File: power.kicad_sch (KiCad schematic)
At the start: 0 parts

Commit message: add comments/todos for each schematics page
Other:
- note added: "Power - PSU-DC/DC Converter - 8-12V->5V: XL1509-5.0E1 - 5->3.3V: SY8113BADCCopy - Automatic Switch between 5V-Extern and 5V-USB"
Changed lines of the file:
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@@
     (company "Juventus Technikerschule")
   )
+  (text "Power\n- PSU-DC/DC Converter\n- 8-12V->5V: XL1509-5.0E1\n- 5->3.3V: SY8113BADCCopy\n- Automatic Switch between 5V-Extern and 5V-USB"
+    (at 13.97 24.13 0)
+    (effects (font (size 1.27 1.27)) (justify left bottom))
+  )
 )

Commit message: updated library, partly created power.kicad_sch
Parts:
- added C? (x3): 10uF, X5R, 25V, C0603, symbol eduboardv2:CL10A106MA8NRNC
- added C? (x3): 220uF, 35V, CAP-SMD_BD8.0-L8.3-W8.3-RD, symbol eduboardv2:VEJ221M1VTR-0810
- added C? (x3): 100nF, 50V, C0402, symbol eduboardv2:CL05B104KB54PNC
- added C? (x2): 1uF, 25V, C0402, symbol eduboardv2:CL05A105KA5NQNC
- added C?: 22pF, C0402, symbol eduboardv2:0402CG220J500NT
- added D?: SS210, SMA_L4.3-W2.6-LS5.2-RD, symbol eduboardv2:SS210
- added IC301: XL1509-5.0E1, SOIC-8_L5.0-W4.0-P1.27-LS6.0-BL, symbol eduboardv2:XL1509-5.0E1
- added L?: 6.8uH, 1A, IND-SMD_L4.0-W4.0, symbol eduboardv2:SWPA4020S6R8MT
- added L?: 68uH, 1A, IND-SMD_L6.0-W6.0_FNR60XXS, symbol eduboardv2:SWPA6045S680MT
- added R? (x2): 5.1k, R0402, symbol eduboardv2:0402WGF5101TCE
- added R? (x2): 100k, R0402, symbol eduboardv2:0402WGF1003TCE
- added R?: 22k, R0402, symbol eduboardv2:0402WGF2202TCE
- added U?: SY8113BADC, TSOT-23-6_L2.9-W1.6-P0.95-LS2.8-BR, symbol eduboardv2:SY8113BADC
- added USBC?: USB3.1C16PFSMT, USB-C-SMD_TYPE-C-USB-17, symbol eduboardv2:USB3.1C16PFSMT
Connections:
- new net: C?.2, L?.1, U?.6 (LX)
- new net: D?.1 (K), IC301.2 (OUTPUT), L?.1
- new net: R?.2, USBC?.A5 (CC1)
- new net: R?.1, USBC?.B5 (CC2)
- new net: C?.1, R?.1, R?.2, U?.3 (FB)
- new net: C?.1, U?.1 (BS)
- new net +3.3V: C?.1, C?.1, C?.1, C?.2, C?.2, L?.2, R?.2
- new net +5V: C?.1, C?.1, C?.1, C?.2, C?.2, IC301.3 (FB), L?.2, R?.2, U?.5 (IN)
- new net 3.3V_EN: R?.1, U?.4 (EN)
- new net GND: C?.1, C?.1, C?.1, C?.2, C?.2, C?.2, C?.2, C?.2, C?.2, C?.2, D?.2 (A), IC301.5 (GND), IC301.6 (GND), IC301.7 (GND), IC301.8 (GND), R?.1, R?.1, R?.2, U?.2 (GND), USBC?.A1 (GND), USBC?.A12 (GND)
- new net V_EXT: C?.1, IC301.1 (VIN)
- new net V_USB: USBC?.A4 (VBUS), USBC?.A9 (VBUS)

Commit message: nearly finished display_ui.kicad_sch and power.kicad_sch
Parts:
- added D? (x2): SS210, SMA_L4.3-W2.6-LS5.2-RD, symbol eduboardv2:SS210
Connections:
- net +5V: now also D?.1 (K), D?.1 (K); no longer C?.1, C?.1, C?.1, C?.2, IC301.3 (FB), L?.2
- net V_USB: now also D?.2 (A)
- new net +5V_EXT: C?.1, C?.1, C?.1, C?.2, D?.2 (A), IC301.3 (FB), L?.2

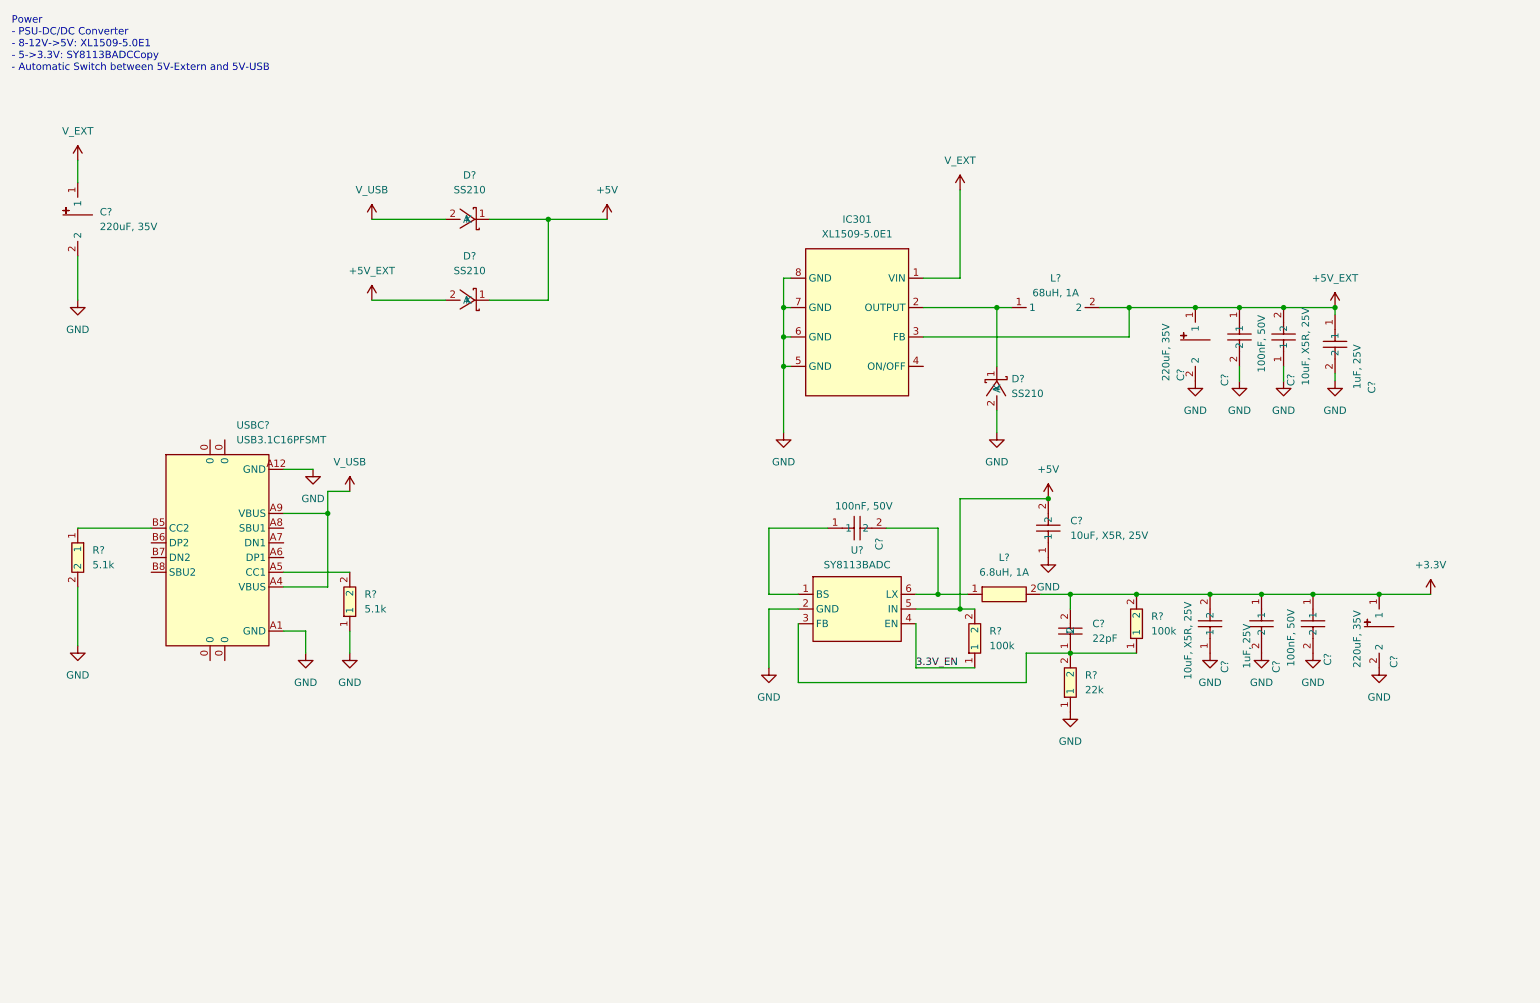
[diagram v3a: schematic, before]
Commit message: added up_rtc_flash.kicad_sch and finished others
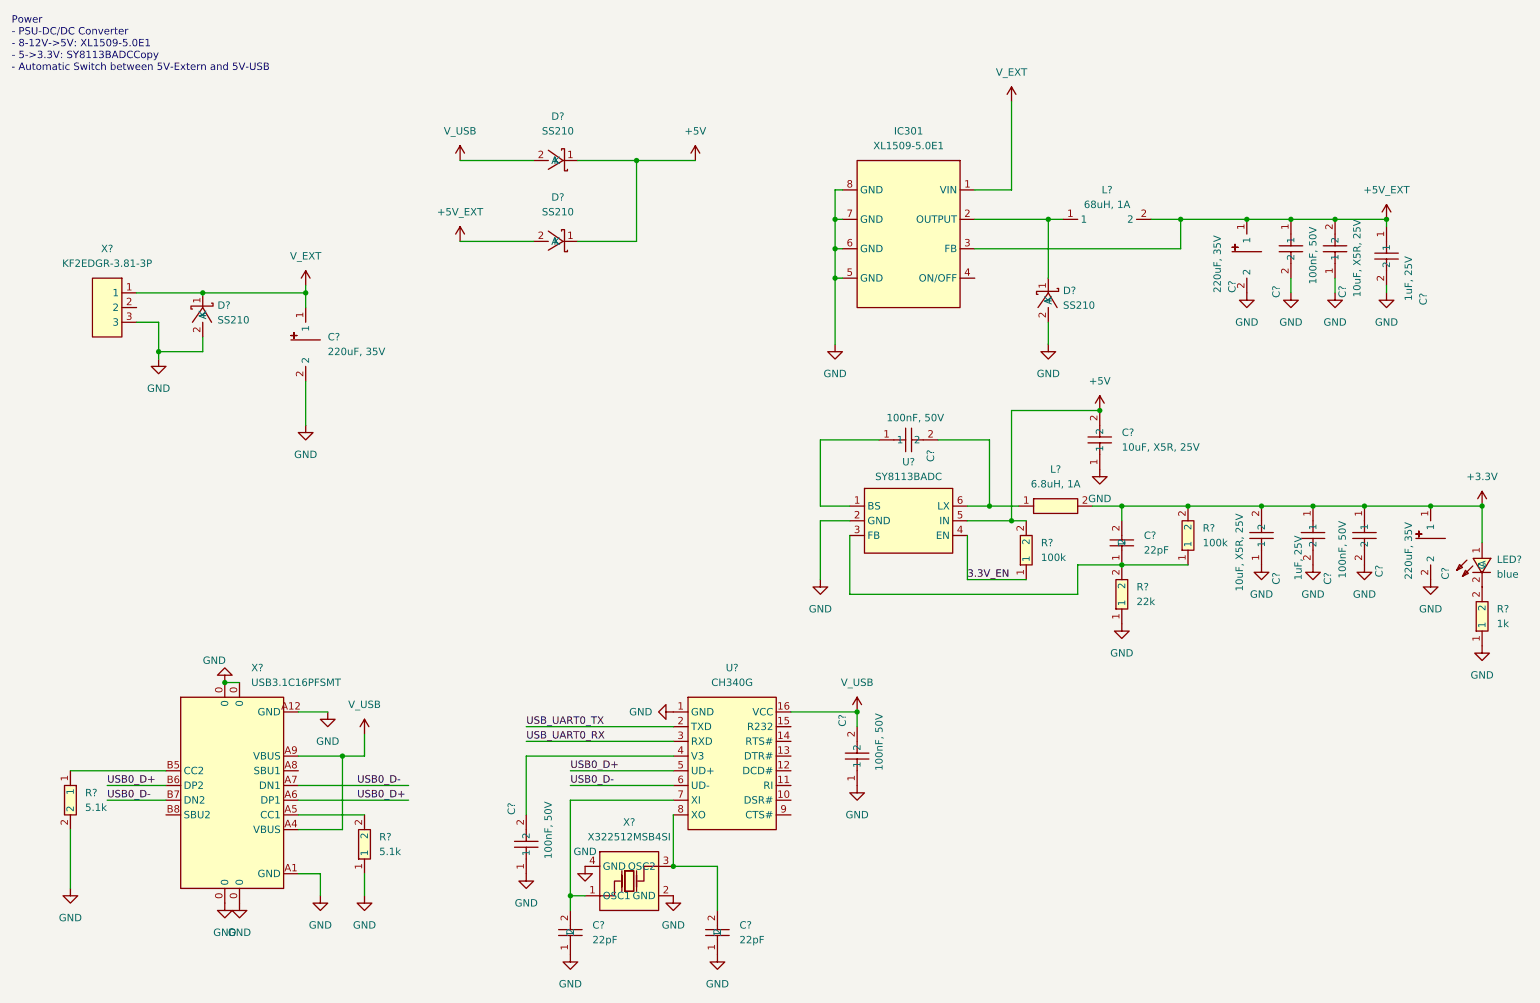
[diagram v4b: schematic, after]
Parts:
- added C? (x2): 100nF, 50V, C0402, symbol eduboardv2:CL05B104KB54PNC
- added C? (x2): 22pF, C0402, symbol eduboardv2:0402CG220J500NT
- added D?: SS210, SMA_L4.3-W2.6-LS5.2-RD, symbol eduboardv2:SS210
- added LED?: blue, LED0603-R-RD_BLUE, symbol eduboardv2:19-217_BHC-ZL1M2RY_3T
- added R?: 1k, R0402, symbol eduboardv2:0402WGF1001TCE
- added U?: CH340G, SOIC-16_L9.9-W3.9-P1.27-LS6.0-BL, symbol eduboardv2:CH340G
- added X?: KF2EDGR-3.81-3P, CONN-TH_3P-P3.81_KF2EDGR-3.81-3P, symbol eduboardv2:KF2EDGR-3.81-3P
- added X?: X322512MSB4SI, OSC-SMD_4P-L3.2-W2.5-BL, symbol eduboardv2:X322512MSB4SI
- gave numbers to parts that had none: 1
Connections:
- net +3.3V: now also LED?.1 (A)
- net GND: now also X?.0, C?.1, C?.1, C?.1, C?.1, D?.2 (A), R?.1, U?.1 (GND), X?.2 (GND), X?.3, X?.4 (GND)
- net V_EXT: now also D?.1 (K), X?.1
- net V_USB: now also C?.2, U?.16 (VCC)
- net USB0_D+: now reaches X?.A6 (DP1)
- net USB0_D+: now also X?.B6 (DP2), U?.5 (UD+)
- net USB0_D-: now reaches X?.A7 (DN1)
- net USB0_D-: now also X?.B7 (DN2), U?.6 (UD-)
- new net: C?.2, U?.4 (V3)
- new net: C?.2, U?.7 (XI), X?.1 (OSC1)
- new net: LED?.2 (C), R?.2
- new net: C?.2, U?.8 (XO), X?.3 (OSC2)
- new net USB_UART0_RX: U?.3 (RXD)
- new net USB_UART0_TX: U?.2 (TXD)
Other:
- moved on the sheet: C?, D?, IC301, L?, R?, U?, X?
